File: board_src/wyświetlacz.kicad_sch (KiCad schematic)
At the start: 5 parts, among them J3 Conn_01x06, Q6 BSS123

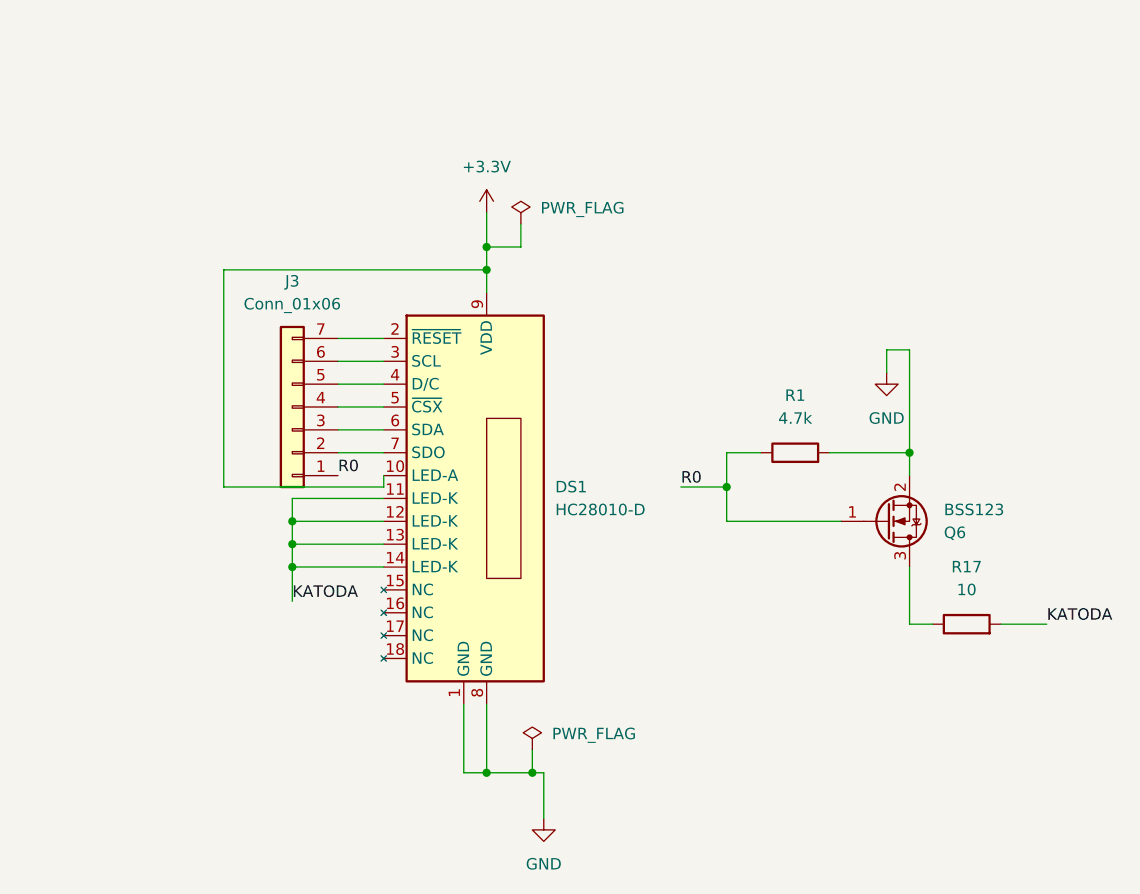
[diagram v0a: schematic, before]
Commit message: Poprawki w schematach. Rozpoczęte korekty płytki
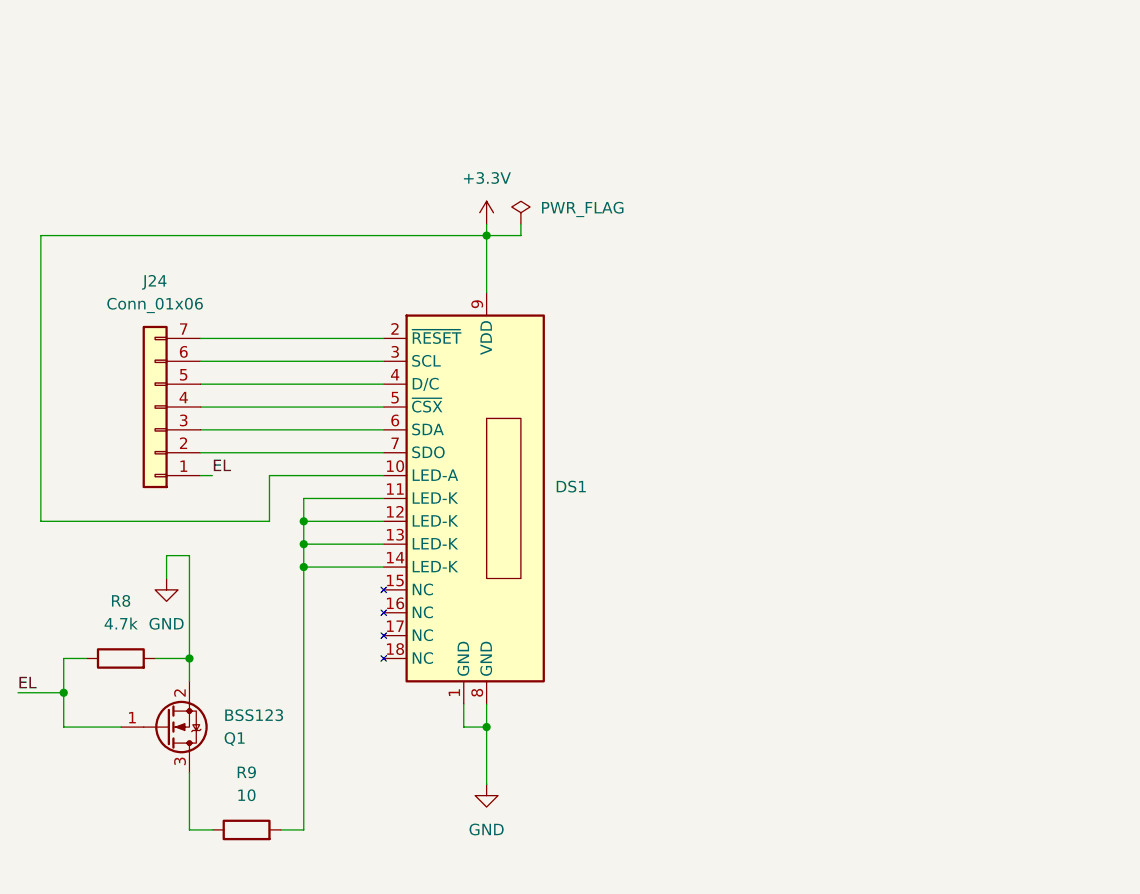
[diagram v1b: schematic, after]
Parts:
- J24: renamed from J3; footprint Connector_PinHeader_2.54mm:PinHeader_1x07_P2.54mm_Vertical -> Connector_PinHeader_2.54mm:PinHeader_1x08_P2.54mm_Vertical
- Q1: renamed from Q6; footprint Package_TO_SOT_SMD:SOT-23 -> Package_TO_SOT_SMD:SOT-23_Handsoldering
- R8: renamed from R1; footprint Resistor_SMD:R_0603_1608Metric -> Resistor_SMD:R_0603_1608Metric_Pad0.98x0.95mm_HandSolder
- R9: renamed from R17; footprint Resistor_SMD:R_0603_1608Metric -> Resistor_SMD:R_0603_1608Metric_Pad0.98x0.95mm_HandSolder
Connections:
- net KATODA: no longer names the net of DS1.11 (LED-K), DS1.12 (LED-K), DS1.13 (LED-K), DS1.14 (LED-K), R9.2
- net R0 renamed EL
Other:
- moved on the sheet: J24, Q1, R8, R9

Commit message: Wprowadzono usprawnienia i poprawki. Wersja ostateczna, wysłana do JLCPCB.
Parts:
- added C11: 100n, Capacitor_SMD:C_0603_1608Metric_Pad1.08x0.95mm_HandSolder, symbol Device:C
- added J44: Conn_01x02, Connector_PinHeader_2.54mm:PinHeader_1x02_P2.54mm_Vertical, symbol Connector_Generic:Conn_01x02
- J24: value Conn_01x06 -> Conn_01x07; footprint Connector_PinHeader_2.54mm:PinHeader_1x08_P2.54mm_Vertical -> Connector_PinHeader_2.54mm:PinHeader_1x07_P2.54mm_Vertical
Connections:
- net +3.3V: now also J44.1 (Pin_1); no longer DS1.10 (LED-A), DS1.9 (VDD)
- net GND: now also C11.2
- new net: C11.1, DS1.10 (LED-A), DS1.9 (VDD), J44.2 (Pin_2)
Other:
- note added: "Zworka zasilania"
